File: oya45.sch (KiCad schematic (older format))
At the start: 108 parts, among them U1 ProMicro

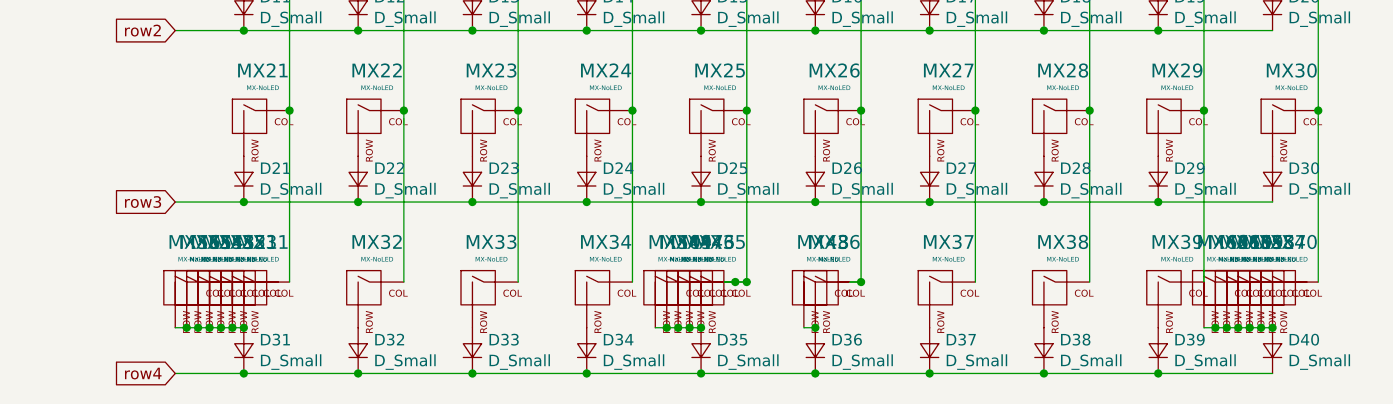
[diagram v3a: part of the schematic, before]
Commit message: added bottom row footprints
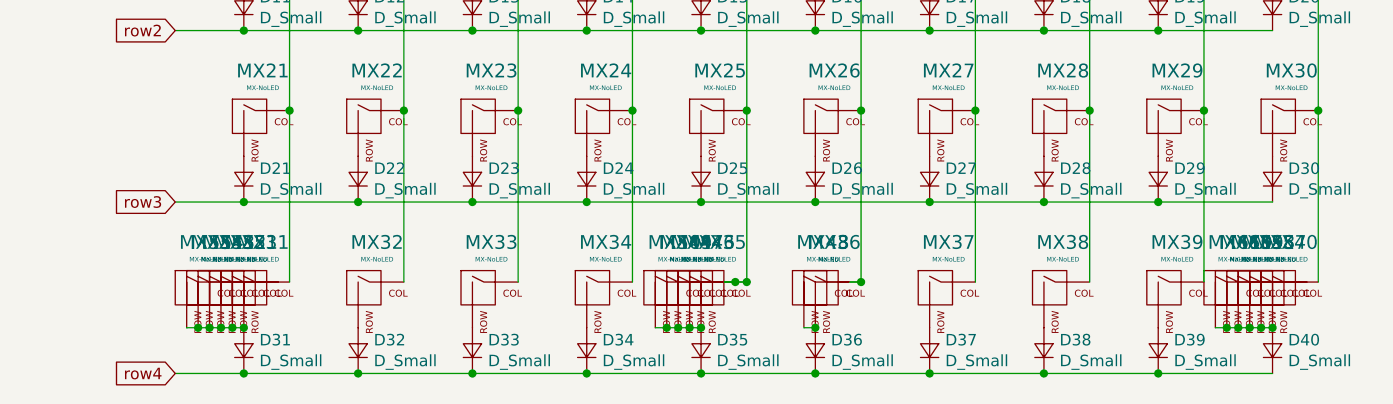
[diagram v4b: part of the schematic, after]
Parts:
- removed MX54, MX60: MX-NoLED, MX_Only:MXOnly-1.5U-NoLED, symbol MX_Alps_Hybrid:MX-NoLED
- MX49: footprint MX_Only:MXOnly-6.25U-ReversedStabilizers-NoLED -> MX_Only:MXOnly-6.25U-ReversedStabilizers-NoSwitch
- MX50: footprint MX_Only:MXOnly-7U-ReversedStabilizers-NoLED -> MX_Only:MXOnly-7U-ReversedStabilizers-NoSwitch
- renumbered MX55 to MX54, MX56 to MX55, MX61 to MX60, MX62 to MX61
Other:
- moved on the sheet: MX54, MX55, MX60, MX61
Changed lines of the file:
@@
 $Comp
 L MX_Alps_Hybrid:MX-NoLED MX54
-U 1 1 61311AAE
+U 1 1 61311CE4
 P 5400 4850
 F 0 "MX54" H 5433 5073 60  0000 C CNN
@@
 $Comp
 L MX_Alps_Hybrid:MX-NoLED MX55
-U 1 1 61311CE4
+U 1 1 61311E89
 P 5350 4850
 F 0 "MX55" H 5383 5073 60  0000 C CNN
@@
 F 3 "" H 4725 4825 60  0001 C CNN
 	1    5350 4850
-	1    0    0    -1
-$EndComp
-$Comp
-L MX_Alps_Hybrid:MX-NoLED MX56
-U 1 1 61311E89
-P 5300 4850
-F 0 "MX56" H 5333 5073 60  0000 C CNN
-F 1 "MX-NoLED" H 5333 4999 20  0000 C CNN
-F 2 "MX_Only:MXOnly-1.5U-NoLED" H 4675 4825 60  0001 C CNN
-F 3 "" H 4675 4825 60  0001 C CNN
-	1    5300 4850
 	1    0    0    -1
 $EndComp
@@
 $Comp
 L MX_Alps_Hybrid:MX-NoLED MX60
-U 1 1 6131279D
+U 1 1 613129F6
 P 9900 4850
 F 0 "MX60" H 9933 5073 60  0000 C CNN
@@
 $Comp
 L MX_Alps_Hybrid:MX-NoLED MX61
-U 1 1 613129F6
+U 1 1 61312BF5
 P 9850 4850
 F 0 "MX61" H 9883 5073 60  0000 C CNN
@@
 $EndComp
 $Comp
-L MX_Alps_Hybrid:MX-NoLED MX62
-U 1 1 61312BF5
-P 9800 4850
-F 0 "MX62" H 9833 5073 60  0000 C CNN
-F 1 "MX-NoLED" H 9833 4999 20  0000 C CNN
-F 2 "MX_Only:MXOnly-1.5U-NoLED" H 9175 4825 60  0001 C CNN
-F 3 "" H 9175 4825 60  0001 C CNN
-	1    9800 4850
-	1    0    0    -1
-$EndComp
-$Comp
 L MX_Alps_Hybrid:MX-NoLED MX49
 U 1 1 61316CF3
@@
 F 0 "MX49" H 7483 5073 60  0000 C CNN
 F 1 "MX-NoLED" H 7483 4999 20  0000 C CNN
-F 2 "MX_Only:MXOnly-6.25U-ReversedStabilizers-NoLED" H 6825 4825 60  0001 C CNN
+F 2 "MX_Only:MXOnly-6.25U-ReversedStabilizers-NoSwitch" H 6825 4825 60  0001 C CNN
 F 3 "" H 6825 4825 60  0001 C CNN
 	1    7450 4850
@@
 F 0 "MX50" H 7433 5073 60  0000 C CNN
 F 1 "MX-NoLED" H 7433 4999 20  0000 C CNN
-F 2 "MX_Only:MXOnly-7U-ReversedStabilizers-NoLED" H 6775 4825 60  0001 C CNN
+F 2 "MX_Only:MXOnly-7U-ReversedStabilizers-NoSwitch" H 6775 4825 60  0001 C CNN
 F 3 "" H 6775 4825 60  0001 C CNN
 	1    7400 4850
@@
 Wire Wire Line
 	7400 5000 7350 5000
-Wire Wire Line
-	5300 5000 5250 5000
-Connection ~ 5300 5000
-Wire Wire Line
-	5350 5000 5300 5000
-Connection ~ 5350 5000
-Wire Wire Line
-	5400 5000 5350 5000
-Connection ~ 5400 5000
-Connection ~ 10050 5000
-Wire Wire Line
-	9800 5000 9750 5000
-Connection ~ 9800 5000
-Wire Wire Line
-	9850 5000 9800 5000
-Connection ~ 9850 5000
-Wire Wire Line
-	9900 5000 9850 5000
-Connection ~ 9900 5000
-Wire Wire Line
-	9950 5000 9900 5000
-Connection ~ 9950 5000
-Wire Wire Line
-	10050 5000 10000 5000
-Wire Wire Line
-	10000 5000 9950 5000
-Connection ~ 10000 5000
-Connection ~ 5550 5000
-Connection ~ 5450 5000
-Wire Wire Line
-	5450 5000 5400 5000
-$Comp
-L MX_Alps_Hybrid:MX-NoLED MX52
-U 1 1 61310BF7
-P 5500 4850
-F 0 "MX52" H 5533 5073 60  0000 C CNN
-F 1 "MX-NoLED" H 5533 4999 20  0000 C CNN
-F 2 "MX_Only:MXOnly-1.25U-NoLED" H 4875 4825 60  0001 C CNN
-F 3 "" H 4875 4825 60  0001 C CNN
-	1    5500 4850
-	1    0    0    -1
-$EndComp
-Connection ~ 5500 5000
-Wire Wire Line
-	5500 5000 5450 5000
-Wire Wire Line
-	5550 5000 5500 5000
 $Comp
 L MX_Alps_Hybrid:MX-NoLED MX51
@@
 	1    0    0    -1
 $EndComp
+$Comp
+L MX_Alps_Hybrid:MX-NoLED MX52
+U 1 1 61310BF7
+P 5500 4850
+F 0 "MX52" H 5533 5073 60  0000 C CNN
+F 1 "MX-NoLED" H 5533 4999 20  0000 C CNN
+F 2 "MX_Only:MXOnly-1.25U-NoLED" H 4875 4825 60  0001 C CNN
+F 3 "" H 4875 4825 60  0001 C CNN
+	1    5500 4850
+	1    0    0    -1
+$EndComp
+Wire Wire Line
+	5550 5000 5500 5000
+Connection ~ 5550 5000
+Connection ~ 5350 5000
+Wire Wire Line
+	5350 5000 5300 5000
+Connection ~ 5400 5000
+Wire Wire Line
+	5400 5000 5350 5000
+Connection ~ 5450 5000
+Wire Wire Line
+	5450 5000 5400 5000
+Connection ~ 5500 5000
+Wire Wire Line
+	5500 5000 5450 5000
+Wire Wire Line
+	10050 5000 10000 5000
+Connection ~ 10050 5000
+Connection ~ 9850 5000
+Wire Wire Line
+	9850 5000 9800 5000
+Connection ~ 9900 5000
+Wire Wire Line
+	9900 5000 9850 5000
+Connection ~ 9950 5000
+Wire Wire Line
+	9950 5000 9900 5000
+Connection ~ 10000 5000
+Wire Wire Line
+	10000 5000 9950 5000
 $EndSCHEMATC

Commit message: finished pcb
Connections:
- net col0: now also MX51.1 (COL), MX52.1 (COL), MX53.1 (COL), MX54.1 (COL), MX55.1 (COL)
- net col9: now also MX57.1 (COL), MX58.1 (COL), MX59.1 (COL), MX60.1 (COL), MX61.1 (COL)
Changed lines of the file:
@@
 Wire Wire Line
 	10000 5000 9950 5000
+Wire Wire Line
+	10250 4800 10200 4800
+Connection ~ 10250 4800
+Connection ~ 10050 4800
+Wire Wire Line
+	10050 4800 10000 4800
+Connection ~ 10100 4800
+Wire Wire Line
+	10100 4800 10050 4800
+Connection ~ 10150 4800
+Wire Wire Line
+	10150 4800 10100 4800
+Connection ~ 10200 4800
+Wire Wire Line
+	10200 4800 10150 4800
+Wire Wire Line
+	5750 4800 5700 4800
+Connection ~ 5750 4800
+Connection ~ 5550 4800
+Wire Wire Line
+	5550 4800 5500 4800
+Connection ~ 5600 4800
+Wire Wire Line
+	5600 4800 5550 4800
+Connection ~ 5650 4800
+Wire Wire Line
+	5650 4800 5600 4800
+Connection ~ 5700 4800
+Wire Wire Line
+	5700 4800 5650 4800
 $EndSCHEMATC

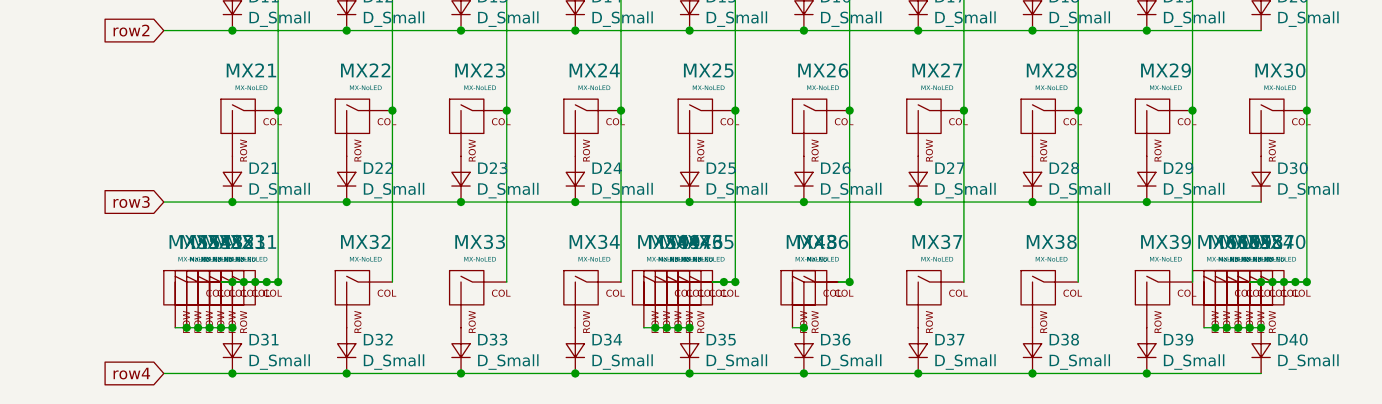
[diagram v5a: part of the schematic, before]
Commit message: cleaned up switch position and tracks, and added gerbers
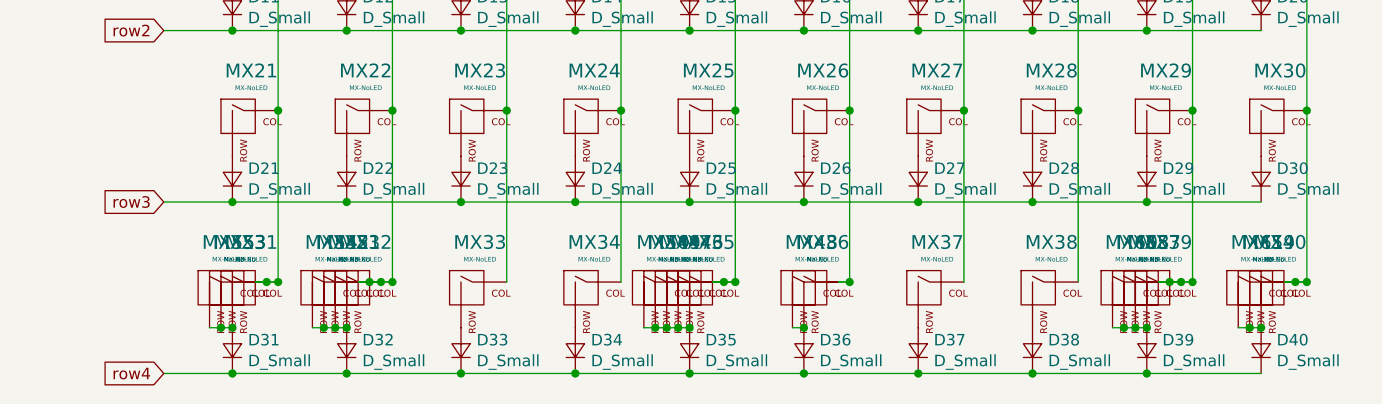
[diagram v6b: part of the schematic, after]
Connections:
- net col0: no longer MX51.1 (COL), MX52.1 (COL), MX54.1 (COL)
- net col1: now also MX51.1 (COL), MX52.1 (COL), MX54.1 (COL)
- net col8: now also MX57.1 (COL), MX58.1 (COL), MX60.1 (COL)
- net col9: no longer MX57.1 (COL), MX58.1 (COL), MX60.1 (COL)
- net at D31.2 (A), MX31.2 (ROW), MX53.2 (ROW)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: no longer MX51.2 (ROW), MX52.2 (ROW), MX54.2 (ROW)
- net at D32.2 (A), MX32.2 (ROW): now also MX51.2 (ROW), MX52.2 (ROW), MX54.2 (ROW)
- net at D39.2 (A), MX39.2 (ROW): now also MX57.2 (ROW), MX58.2 (ROW), MX60.2 (ROW)
- net at D40.2 (A), MX40.2 (ROW), MX59.2 (ROW)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: no longer MX57.2 (ROW), MX58.2 (ROW), MX60.2 (ROW)
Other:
- moved on the sheet: MX51, MX52, MX53, MX54, MX55, MX57, MX58, MX59, MX60, MX61
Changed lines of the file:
@@
-$EndComp
-$Comp
-L MX_Alps_Hybrid:MX-NoLED MX32
-U 1 1 612DA588
-P 6100 4850
-F 0 "MX32" H 6133 5073 60  0000 C CNN
-F 1 "MX-NoLED" H 6133 4999 20  0000 C CNN
-F 2 "MX_Only:MXOnly-1U-NoLED" H 5475 4825 60  0001 C CNN
-F 3 "" H 5475 4825 60  0001 C CNN
-	1    6100 4850
-	1    0    0    -1
 $EndComp
 $Comp
@@
 Connection ~ 7750 2550
 $Comp
-L MX_Alps_Hybrid:MX-NoLED MX54
-U 1 1 61311CE4
-P 5400 4850
-F 0 "MX54" H 5433 5073 60  0000 C CNN
-F 1 "MX-NoLED" H 5433 4999 20  0000 C CNN
-F 2 "MX_Only:MXOnly-1.5U-NoLED" H 4775 4825 60  0001 C CNN
-F 3 "" H 4775 4825 60  0001 C CNN
-	1    5400 4850
-	1    0    0    -1
-$EndComp
-$Comp
-L MX_Alps_Hybrid:MX-NoLED MX55
-U 1 1 61311E89
-P 5350 4850
-F 0 "MX55" H 5383 5073 60  0000 C CNN
-F 1 "MX-NoLED" H 5383 4999 20  0000 C CNN
-F 2 "MX_Only:MXOnly-1.5U-NoLED" H 4725 4825 60  0001 C CNN
-F 3 "" H 4725 4825 60  0001 C CNN
-	1    5350 4850
-	1    0    0    -1
-$EndComp
-$Comp
 L MX_Alps_Hybrid:MX-NoLED MX57
 U 1 1 6131203D
+P 9550 4850
+F 0 "MX57" H 9583 5073 60  0000 C CNN
+F 1 "MX-NoLED" H 9583 4999 20  0000 C CNN
+F 2 "MX_Only:MXOnly-1.25U-NoLED" H 8925 4825 60  0001 C CNN
+F 3 "" H 8925 4825 60  0001 C CNN
+	1    9550 4850
+	1    0    0    -1
+$EndComp
+$Comp
+L MX_Alps_Hybrid:MX-NoLED MX58
+U 1 1 6131231D
+P 9500 4850
+F 0 "MX58" H 9533 5073 60  0000 C CNN
+F 1 "MX-NoLED" H 9533 4999 20  0000 C CNN
+F 2 "MX_Only:MXOnly-1.25U-NoLED" H 8875 4825 60  0001 C CNN
+F 3 "" H 8875 4825 60  0001 C CNN
+	1    9500 4850
+	1    0    0    -1
+$EndComp
+$Comp
+L MX_Alps_Hybrid:MX-NoLED MX59
+U 1 1 6131254E
 P 10050 4850
-F 0 "MX57" H 10083 5073 60  0000 C CNN
+F 0 "MX59" H 10083 5073 60  0000 C CNN
 F 1 "MX-NoLED" H 10083 4999 20  0000 C CNN
 F 2 "MX_Only:MXOnly-1.25U-NoLED" H 9425 4825 60  0001 C CNN
@@
 $EndComp
 $Comp
-L MX_Alps_Hybrid:MX-NoLED MX58
-U 1 1 6131231D
+L MX_Alps_Hybrid:MX-NoLED MX60
+U 1 1 613129F6
+P 9450 4850
+F 0 "MX60" H 9483 5073 60  0000 C CNN
+F 1 "MX-NoLED" H 9483 4999 20  0000 C CNN
+F 2 "MX_Only:MXOnly-1.5U-NoLED" H 8825 4825 60  0001 C CNN
+F 3 "" H 8825 4825 60  0001 C CNN
+	1    9450 4850
+	1    0    0    -1
+$EndComp
+$Comp
+L MX_Alps_Hybrid:MX-NoLED MX61
+U 1 1 61312BF5
 P 10000 4850
-F 0 "MX58" H 10033 5073 60  0000 C CNN
+F 0 "MX61" H 10033 5073 60  0000 C CNN
 F 1 "MX-NoLED" H 10033 4999 20  0000 C CNN
-F 2 "MX_Only:MXOnly-1.25U-NoLED" H 9375 4825 60  0001 C CNN
+F 2 "MX_Only:MXOnly-1.5U-NoLED" H 9375 4825 60  0001 C CNN
 F 3 "" H 9375 4825 60  0001 C CNN
 	1    10000 4850
-	1    0    0    -1
-$EndComp
-$Comp
-L MX_Alps_Hybrid:MX-NoLED MX59
-U 1 1 6131254E
-P 9950 4850
-F 0 "MX59" H 9983 5073 60  0000 C CNN
-F 1 "MX-NoLED" H 9983 4999 20  0000 C CNN
-F 2 "MX_Only:MXOnly-1.25U-NoLED" H 9325 4825 60  0001 C CNN
-F 3 "" H 9325 4825 60  0001 C CNN
-	1    9950 4850
-	1    0    0    -1
-$EndComp
-$Comp
-L MX_Alps_Hybrid:MX-NoLED MX60
-U 1 1 613129F6
-P 9900 4850
-F 0 "MX60" H 9933 5073 60  0000 C CNN
-F 1 "MX-NoLED" H 9933 4999 20  0000 C CNN
-F 2 "MX_Only:MXOnly-1.5U-NoLED" H 9275 4825 60  0001 C CNN
-F 3 "" H 9275 4825 60  0001 C CNN
-	1    9900 4850
-	1    0    0    -1
-$EndComp
-$Comp
-L MX_Alps_Hybrid:MX-NoLED MX61
-U 1 1 61312BF5
-P 9850 4850
-F 0 "MX61" H 9883 5073 60  0000 C CNN
-F 1 "MX-NoLED" H 9883 4999 20  0000 C CNN
-F 2 "MX_Only:MXOnly-1.5U-NoLED" H 9225 4825 60  0001 C CNN
-F 3 "" H 9225 4825 60  0001 C CNN
-	1    9850 4850
 	1    0    0    -1
 $EndComp
@@
 L MX_Alps_Hybrid:MX-NoLED MX51
 U 1 1 6130DEB4
+P 6050 4850
+F 0 "MX51" H 6083 5073 60  0000 C CNN
+F 1 "MX-NoLED" H 6083 4999 20  0000 C CNN
+F 2 "MX_Only:MXOnly-1.25U-NoLED" H 5425 4825 60  0001 C CNN
+F 3 "" H 5425 4825 60  0001 C CNN
+	1    6050 4850
+	1    0    0    -1
+$EndComp
+$Comp
+L MX_Alps_Hybrid:MX-NoLED MX52
+U 1 1 61310BF7
+P 6000 4850
+F 0 "MX52" H 6033 5073 60  0000 C CNN
+F 1 "MX-NoLED" H 6033 4999 20  0000 C CNN
+F 2 "MX_Only:MXOnly-1.25U-NoLED" H 5375 4825 60  0001 C CNN
+F 3 "" H 5375 4825 60  0001 C CNN
+	1    6000 4850
+	1    0    0    -1
+$EndComp
+$Comp
+L MX_Alps_Hybrid:MX-NoLED MX53
+U 1 1 6131191D
 P 5550 4850
-F 0 "MX51" H 5583 5073 60  0000 C CNN
+F 0 "MX53" H 5583 5073 60  0000 C CNN
 F 1 "MX-NoLED" H 5583 4999 20  0000 C CNN
 F 2 "MX_Only:MXOnly-1.25U-NoLED" H 4925 4825 60  0001 C CNN
@@
 $EndComp
 $Comp
-L MX_Alps_Hybrid:MX-NoLED MX53
-U 1 1 6131191D
-P 5450 4850
-F 0 "MX53" H 5483 5073 60  0000 C CNN
-F 1 "MX-NoLED" H 5483 4999 20  0000 C CNN
-F 2 "MX_Only:MXOnly-1.25U-NoLED" H 4825 4825 60  0001 C CNN
-F 3 "" H 4825 4825 60  0001 C CNN
-	1    5450 4850
-	1    0    0    -1
-$EndComp
-$Comp
-L MX_Alps_Hybrid:MX-NoLED MX52
-U 1 1 61310BF7
+L MX_Alps_Hybrid:MX-NoLED MX55
+U 1 1 61311E89
 P 5500 4850
-F 0 "MX52" H 5533 5073 60  0000 C CNN
+F 0 "MX55" H 5533 5073 60  0000 C CNN
 F 1 "MX-NoLED" H 5533 4999 20  0000 C CNN
-F 2 "MX_Only:MXOnly-1.25U-NoLED" H 4875 4825 60  0001 C CNN
+F 2 "MX_Only:MXOnly-1.5U-NoLED" H 4875 4825 60  0001 C CNN
 F 3 "" H 4875 4825 60  0001 C CNN
 	1    5500 4850
 	1    0    0    -1
 $EndComp
+$Comp
+L MX_Alps_Hybrid:MX-NoLED MX54
+U 1 1 61311CE4
+P 5950 4850
+F 0 "MX54" H 5983 5073 60  0000 C CNN
+F 1 "MX-NoLED" H 5983 4999 20  0000 C CNN
+F 2 "MX_Only:MXOnly-1.5U-NoLED" H 5325 4825 60  0001 C CNN
+F 3 "" H 5325 4825 60  0001 C CNN
+	1    5950 4850
+	1    0    0    -1
+$EndComp
+$Comp
+L MX_Alps_Hybrid:MX-NoLED MX32
+U 1 1 612DA588
+P 6100 4850
+F 0 "MX32" H 6133 5073 60  0000 C CNN
+F 1 "MX-NoLED" H 6133 4999 20  0000 C CNN
+F 2 "MX_Only:MXOnly-1U-NoLED" H 5475 4825 60  0001 C CNN
+F 3 "" H 5475 4825 60  0001 C CNN
+	1    6100 4850
+	1    0    0    -1
+$EndComp
+Wire Wire Line
+	6250 4800 6200 4800
+Connection ~ 6250 4800
+Connection ~ 6150 4800
+Wire Wire Line
+	6150 4800 6100 4800
+Connection ~ 6200 4800
+Wire Wire Line
+	6200 4800 6150 4800
+Wire Wire Line
+	5750 4800 5700 4800
+Connection ~ 5750 4800
+Connection ~ 5700 4800
+Wire Wire Line
+	5700 4800 5650 4800
+Wire Wire Line
+	6050 5000 6000 5000
+Connection ~ 6050 5000
+Connection ~ 5950 5000
+Wire Wire Line
+	5950 5000 5900 5000
+Connection ~ 6000 5000
+Wire Wire Line
+	6000 5000 5950 5000
 Wire Wire Line
 	5550 5000 5500 5000
 Connection ~ 5550 5000
-Connection ~ 5350 5000
-Wire Wire Line
-	5350 5000 5300 5000
-Connection ~ 5400 5000
-Wire Wire Line
-	5400 5000 5350 5000
-Connection ~ 5450 5000
-Wire Wire Line
-	5450 5000 5400 5000
 Connection ~ 5500 5000
 Wire Wire Line
 	5500 5000 5450 5000
+Wire Wire Line
+	10250 4800 10200 4800
+Connection ~ 10250 4800
+Connection ~ 10200 4800
+Wire Wire Line
+	10200 4800 10150 4800
 Wire Wire Line
 	10050 5000 10000 5000
 Connection ~ 10050 5000
-Connection ~ 9850 5000
-Wire Wire Line
-	9850 5000 9800 5000
-Connection ~ 9900 5000
-Wire Wire Line
-	9900 5000 9850 5000
-Connection ~ 9950 5000
-Wire Wire Line
-	9950 5000 9900 5000
 Connection ~ 10000 5000
 Wire Wire Line
 	10000 5000 9950 5000
 Wire Wire Line
-	10250 4800 10200 4800
-Connection ~ 10250 4800
-Connection ~ 10050 4800
-Wire Wire Line
-	10050 4800 10000 4800
-Connection ~ 10100 4800
-Wire Wire Line
-	10100 4800 10050 4800
-Connection ~ 10150 4800
-Wire Wire Line
-	10150 4800 10100 4800
-Connection ~ 10200 4800
-Wire Wire Line
-	10200 4800 10150 4800
-Wire Wire Line
-	5750 4800 5700 4800
-Connection ~ 5750 4800
-Connection ~ 5550 4800
-Wire Wire Line
-	5550 4800 5500 4800
-Connection ~ 5600 4800
-Wire Wire Line
-	5600 4800 5550 4800
-Connection ~ 5650 4800
-Wire Wire Line
-	5650 4800 5600 4800
-Connection ~ 5700 4800
-Wire Wire Line
-	5700 4800 5650 4800
+	9750 4800 9700 4800
+Connection ~ 9750 4800
+Connection ~ 9650 4800
+Wire Wire Line
+	9650 4800 9600 4800
+Connection ~ 9700 4800
+Wire Wire Line
+	9700 4800 9650 4800
+Wire Wire Line
+	9550 5000 9500 5000
+Connection ~ 9550 5000
+Connection ~ 9450 5000
+Wire Wire Line
+	9450 5000 9400 5000
+Connection ~ 9500 5000
+Wire Wire Line
+	9500 5000 9450 5000
 $EndSCHEMATC
